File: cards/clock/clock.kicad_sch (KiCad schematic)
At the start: 54 parts, among them J1 BUS, J2 SLOW, Q1 2N7000, Q10 2N7000, Q11 2N7000, Q12 2N7000, Q13 2N7000, Q14 2N7000, Q15 2N7000, Q16 2N7000, Q2 2N7000, Q3 2N7000, Q4 2N7000, Q5 2N7000, Q6 2N7000, Q7 2N7000, Q8 2N7000, Q9 2N7000, SW1 RUN

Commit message: Clock and panel: CLK and RST driven hard, the cards see one clock edge (D053)
The memory address latch race (D054, next commit) had a root under it:
the clock card's CLK pull-up was 10k into about 3 nF of card inputs and
ribbon, so the rising edge took 35 to 43 us from 0.5 to 3.5 V, and every
card reads that edge with its own transistors (Vto 0.8 to 3.0 V), so the
cards saw one edge up to 25 us apart. At mixed seed 2 the sequencer stepped
at 2 V and a register put the next tick's data on the bus 10 us later,
while the memory control card saw the edge at 3 V, 12 us after the bus had
changed. RST had the same trouble the other way: driven through 10k
against the panel's 1 Meg, it drifted for 8 ms after the reset Schmitt
let go (the machine once started a tick late, memory nibble-v2-plan
2026-09-14), so cards with different thresholds left reset on different
edges.

cards/clock (re-routed, DRC 0, 0 unconnected): the CLK pull-up is 1k, and
RST comes from a new inverter RD = NOT PB with a 1k pull-up through 100 ohm
and a diode. Lowering PA's own 47k instead took the gain out of the reset
Schmitt and RST followed the 220 ms capacitor ramp for milliseconds; the
buffer keeps the snap. cards/panela, panelb (values only, no layout
change): the CLK and RST pull-downs are 10k, the buttons' Schmitt output
inverters have 1k pull-ups and drive the lines through 100 ohm. About
20 mA more from the supply.

tb_clock now loads both lines with 3 nF and the panel's 10k, drives the
STEP button as the panel does, and measures CLK's rise (0.5 to 3.5 V,
must be under 10 us) and RST's release (3.5 to 0.8 V, under 100 us). On
the routed card's export: CLK rise 5.3 to 6.7 us, RST release 44 to 46 us,
period and duty unchanged (610 Hz TYP, 404 LO, 582 HI), one edge per STEP
press, at TYP, LO, HI, MIX 1 and 2, all PASS (sim/out/tb_clock_cards54_*.log).
The previous card on the same bench: CLK rise 43 us, RST never reached
0.8 V cleanly (sim/out/tb_clock_cards_oldD053_TYP.log).

machine.py: a dec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
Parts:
- added Q17: 2N7000, Package_TO_SOT_THT:TO-92_Inline_Wide, symbol Transistor_FET:2N7000
- added R23: 100, Resistor_THT:R_Axial_DIN0207_L6.3mm_D2.5mm_P5.08mm_Vertical, symbol Device:R
- R12: value 47k -> 1k
- R13: value 10k -> 47k
- R14: value 1k -> 10k
- R15, R18: value 100k -> 1k
- R16, R21: value 1Meg -> 100k
- R17, R22: value 10k -> 1Meg
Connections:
- net +5V: now also R12.2, R14.1, R20.1; no longer R12.1, R19.1
- net CLK: now also R18.2; no longer R17.2
- net GND: now also Q15.1 (S), R15.2, R17.2; no longer R14.2, R16.2
- net HLT: now also R19.1; no longer R18.1
- net HLTD: now also R19.2; no longer R18.2
- net PA: no longer R22.1
- net PB: now also Q13.2 (G), R22.1; no longer R21.1
- net PN: now also R22.2; no longer R20.2
- net POR: now also R20.2, R21.1; no longer R19.2, R20.1
- net RT: now also R16.2; no longer R15.2
- net RUNSW: now also Q14.2 (G), R17.1; no longer Q13.2 (G), R16.1
- net SA: now also R16.1; no longer R15.1
- net SB: now also Q15.2 (G); no longer Q14.2 (G)
- net VD2: now also R14.2, Q17.3 (D); no longer Q16.3 (D), R13.2
- net VS: now also R15.1, Q17.1 (S); no longer Q15.1 (S), R14.1
- net X: now also Q16.2 (G); no longer Q15.2 (G)
- net at D1.1 (K): now also Q14.3 (D); no longer Q13.3 (D)
- net at D2.1 (K): now also Q15.3 (D); no longer Q14.3 (D)
- net at D1.2 (A): now also R11.2; no longer R10.1
- net at D4.2 (A): now also R23.2; no longer R22.2
- net at D3.1 (K): now also R18.1; no longer R17.1
- net at D2.2 (A): now also R12.1; no longer R11.2
- new net: Q16.3 (D), Q17.2 (G), R13.2
- new net RD: Q13.3 (D), R10.1, R23.1
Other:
- note added: "17 transistors, 21 resistors, 2 LEDs, one pot, one switch, one jumper, 100 x 100 mm (docs/cards.md). RUN: the switch puts 1k from +5V on CLK (a few microseconds into the 3 nF of cards and ribbon, D053) and the oscillator pulls CLK low for half of each cycle, or for as long as HLT is high. STEP: the switch is open and the pull-down transistor is held off; the front panel's CLK button owns the line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"
- note added: "POWER-ON RESET SCHMITT: PA = NOT PN, PB = NOT PA; PN is the RC node through 100k with 1 Meg from PB (drawn on the sheet). While PA is high (the capacitor still low) RD = NOT PB, a 1k pull-up, drives RST through 100 ohm and a diode; the panel's 10k pull-down releases it in tens of microseconds (D053)"
- note added: "POWER-ON RESET: POR charges through 100k into 2.2 uF; 100k into PN with 1 Meg from PB (hysteresis); RD = NOT PB (high while the capacitor is still low, 1k pull-up) drives RST through 100 ohm and a diode against the panel's 10k pull-down (D053)"
- note added: "RUN / STEP: the switch closes +5V onto RUNSW (1 Meg pull-down); a diode and 1k from RUNSW to CLK are the clock's pull-up, present only in RUN (1k, D053: the rising edge into the cards' 3 nF takes microseconds, not 35)"
- note removed: "16 transistors, 20 resistors, 2 LEDs, one pot, one switch, one jumper, 100 x 100 mm (docs/cards.md). RUN: the switch puts 10k from +5V on CLK and the oscillator pulls CLK low for half of each cycle, or for as long as HLT is high. STEP: the switch is open and the pull-down transistor is held off; the front panel's CLK button owns the line, one edge per press. Speed: a Schmitt-trigger RC oscillator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"
- note removed: "POWER-ON RESET SCHMITT: PA = NOT PN, PB = NOT PA; PN is the RC node through 100k with 1 Meg from PB (drawn on the sheet). While PA is high (the capacitor still low) RST is pulled high through 10k and a diode"
- note removed: "POWER-ON RESET: POR charges through 100k into 2.2 uF; 100k into PN with 1 Meg from PB (hysteresis); PA (high while the capacitor is still low) drives RST through 10k and a diode"
- note removed: "RUN / STEP: the switch closes +5V onto RUNSW (1 Meg pull-down); a diode and 10k from RUNSW to CLK are the clock's pull-up, present only in RUN"

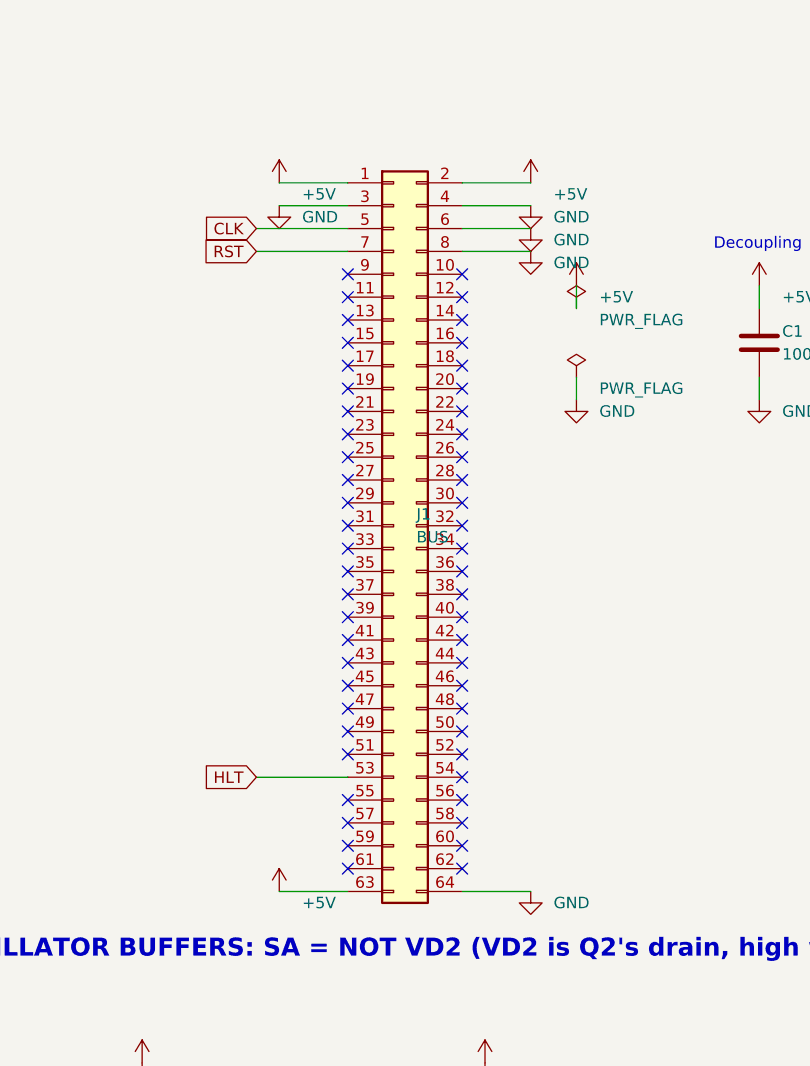
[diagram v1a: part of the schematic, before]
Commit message: The bus headers go on the back of all 26 boards, no track moved; the silkscreen refitted (D059, D062)
An IDC socket lies across its ribbon, so the ribbon could never run along a
row of cards as drawn. It runs behind them, and the 64-pin headers are
soldered on the back. This commit is that move, made in place on the routed
boards: no board was routed again.

How the header sits (D062): in the holes it had, turned over top to bottom,
notch toward the top edge. A pin of the odd row is then in the hole its even
neighbour had, so the two signals of every pair of pins change places: CLK
is pin 6, RST pin 8, +5V pins 1, 2 and 64. bus.py keeps both tables: PINS,
what the header's pins carry, and HOLES, what the copper was routed to.

The proof, on all 26 boards against 992a90f (sim/board_diff.py):
  netlist the same, element for element; every track, every via and every
  hole the same; each copper and mask layer differs by two pad shapes per
  header (pin 1's square went to the hole beside it, both on +5V) and the
  ground pour's outline round those two pads, nowhere else by more than a
  tenth of a micrometre.
sim/rebuild_check.py runs every builder into a scratch directory: each
writes the plan and the netlist that are committed, so a rebuild gives
this board. order_check.py --machine holds every pad of the 27 headers to
bus.py and requires them on the back.

What the move costs: on the ribbon RST had a ground conductor on both
sides; now one neighbour is BUS1#. tb_rst_neighbour.py puts the two lines
on the bench with every gate the routed boards hang on them: RST rises
0.28 to 0.43 V when BUS1# is released, against a lowest threshold of 0.8 V
(sim/results/rst_neighbour.md). The machine deck's crosstalk option now
couples the pins that are neighbours on the ribbon; the crosstalk stage of
the machine gate has to be run again on that order.

Silkscreen (pcb.fit_silk): every label to 1.0 mm where it has room, off
pads, vias, outlines and other labels, out from under the pa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
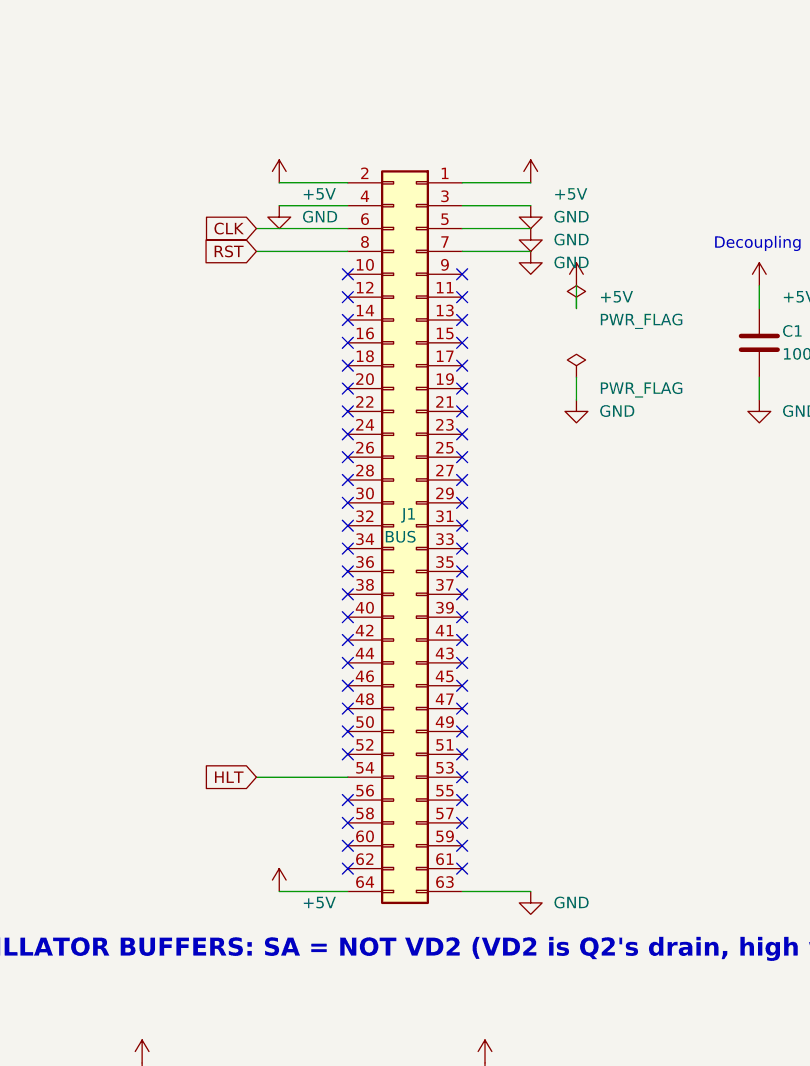
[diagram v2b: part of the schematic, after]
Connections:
- net +5V: now also J1.64 (Pin_64); no longer J1.63 (Pin_63)
- net CLK: now also J1.6 (Pin_6); no longer J1.5 (Pin_5)
- net GND: now also J1.5 (Pin_5), J1.63 (Pin_63), J1.7 (Pin_7); no longer J1.6 (Pin_6), J1.64 (Pin_64), J1.8 (Pin_8)
- net HLT: now also J1.54 (Pin_54); no longer J1.53 (Pin_53)
- net RST: now also J1.8 (Pin_8); no longer J1.7 (Pin_7)
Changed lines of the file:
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@@
 	(symbol
 		(lib_id "Connector_Generic:Conn_02x32_Odd_Even")
-		(at 76.2 101.6 0)
+		(at 78.74 101.6 0)
+		(mirror y)
 		(unit 1)
 		(body_style 1)

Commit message: Clock card: the hold-off is on the card (D064); the machine's deck is the one the 74 runs proved
sim/build_clock_card.py adds the two parts of D064: Q18, a 2N7000 with its
gate on the RST line, its drain through R24, 100 ohm, to the oscillator's
timing node X, its source on the tiles' ground trunk, which is extended
down to it (routed once without that, the pour left the source pad on an
island of its own). The card's export is the one before plus
  MQ18 Net-_Q18-D_ RST GND 2N7000
  R24 X Net-_Q18-D_ 100
and nothing else. Routed in one attempt, DRC clean, every label at 1.0 mm.
The print, the two renders and the assembly drawing looked at.

The machine deck built from this card is the deck the queue ran with
HOLD=1, element for element: the clock's subcircuit the same with the two
parts' names changed, the rest of the deck the same (checked against the
saved deck of the MIX2 start at POR_V0 3.133881 V). So the 62 starts
(sim/results/starts_hold.md) and the 12 crosstalk runs
(sim/results/gate26_cross.md) are this card's.

The order: one more 2N7000 (3516) and one more 100 ohm (6); the buy
column does not move. docs: cards.md, cards/README.md, DECISIONS.md D064
(on the card), audit.md (the crosstalk stage paid, the part counts).

Co-Authored-By: Claude Fable 5.1 <noreply@anthropic.com>
Claude-Session: https://claude.ai/code/session_01RktbhdQjDu7SpFpvkevyUU
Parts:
- added Q18: 2N7000, Package_TO_SOT_THT:TO-92_Inline_Wide, symbol Transistor_FET:2N7000
- added R24: 100, Resistor_THT:R_Axial_DIN0207_L6.3mm_D2.5mm_P5.08mm_Vertical, symbol Device:R
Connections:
- net GND: now also Q18.1 (S)
- net RST: now also Q18.2 (G)
- net X: now also R24.1
- new net: Q18.3 (D), R24.2
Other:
- note added: "18 transistors, 22 resistors, 2 LEDs, one pot, one switch, one jumper, 100 x 100 mm (docs/cards.md). RUN: the switch puts 1k from +5V on CLK (a few microseconds into the 3 nF of cards and ribbon, D053) and the oscillator pulls CLK low for half of each cycle, or for as long as HLT is high. STEP: the switch is open and the pull-down transistor is held off; the front panel's CLK button owns the line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"
- note added: "HOLD-OFF (D064): while RST is high this transistor holds X at 0 V through 100 ohm: the Schmitt trigger reads low and the clock gate holds CLK low. When RST lets go, the card's own reset or the panel's button, X charges from 0 V and the first clock edge comes 1.3 to 5.4 ms later at the fastest setting, never in the 45 us in which the cards leave their resets"
- note removed: "17 transistors, 21 resistors, 2 LEDs, one pot, one switch, one jumper, 100 x 100 mm (docs/cards.md). RUN: the switch puts 1k from +5V on CLK (a few microseconds into the 3 nF of cards and ribbon, D053) and the oscillator pulls CLK low for half of each cycle, or for as long as HLT is high. STEP: the switch is open and the pull-down transistor is held off; the front panel's CLK button owns the line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"

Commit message: Clock card: the pot's leg holes for the Bourns PTV09A-4; pcb.py --refit
The Alpha RD901F-40 the card was drawn for is not at DigiKey or LCSC; the
Bourns PTV09A-4020F-B105 (1 M linear, 9 mm, shaft up) is, with the same
three pins 2.5 mm apart and its two mounting legs 8.8 mm apart, 7.0 mm
behind the pins, in 2.2 mm holes (the Alpha's are slots 9.6 mm apart,
7.5 mm back). lib/nibble.pretty gets the footprint, drawn from the
maker's recommended layout; pin 1 the counter-clockwise end as before.

pcb.py --refit REF puts the footprint the schematic now names into a
placed part's holes on a routed board: every numbered pad must land
where the old one was and keeps its net, so the copper is untouched (only
the GND pour backs away from the two new leg pads); DRC 0, 0 unconnected,
fab outputs regenerated. The clock card was not in the pilot order.

ksch.write_fp_lib_table: the project's own library table, written by the
hub's and now the clock's builder. bom.py, order-1.md and audit.md name
the Bourns part; rebuild_check clock hub: the builders write what is
committed; bom --check and the pins selftest pass.

Co-Authored-By: Claude Fable 5.1 <noreply@anthropic.com>
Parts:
- RV1: footprint Potentiometer_THT:Potentiometer_Alpha_RD901F-40-00D_Single_Vertical -> nibble:Potentiometer_Bourns_PTV09A-4_Single_Vertical
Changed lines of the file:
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@@
 			)
 		)
-		(property "Footprint" "Potentiometer_THT:Potentiometer_Alpha_RD901F-40-00D_Single_Vertical"
+		(property "Footprint" "nibble:Potentiometer_Bourns_PTV09A-4_Single_Vertical"
 			(at 60.96 477.52 0)
 			(hide yes)
